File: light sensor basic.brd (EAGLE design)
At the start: 83.2 x 57.8 mm, 13 parts, among them J1 UJ2-MIBH-G-SMT-TR, U1 VCNT2020

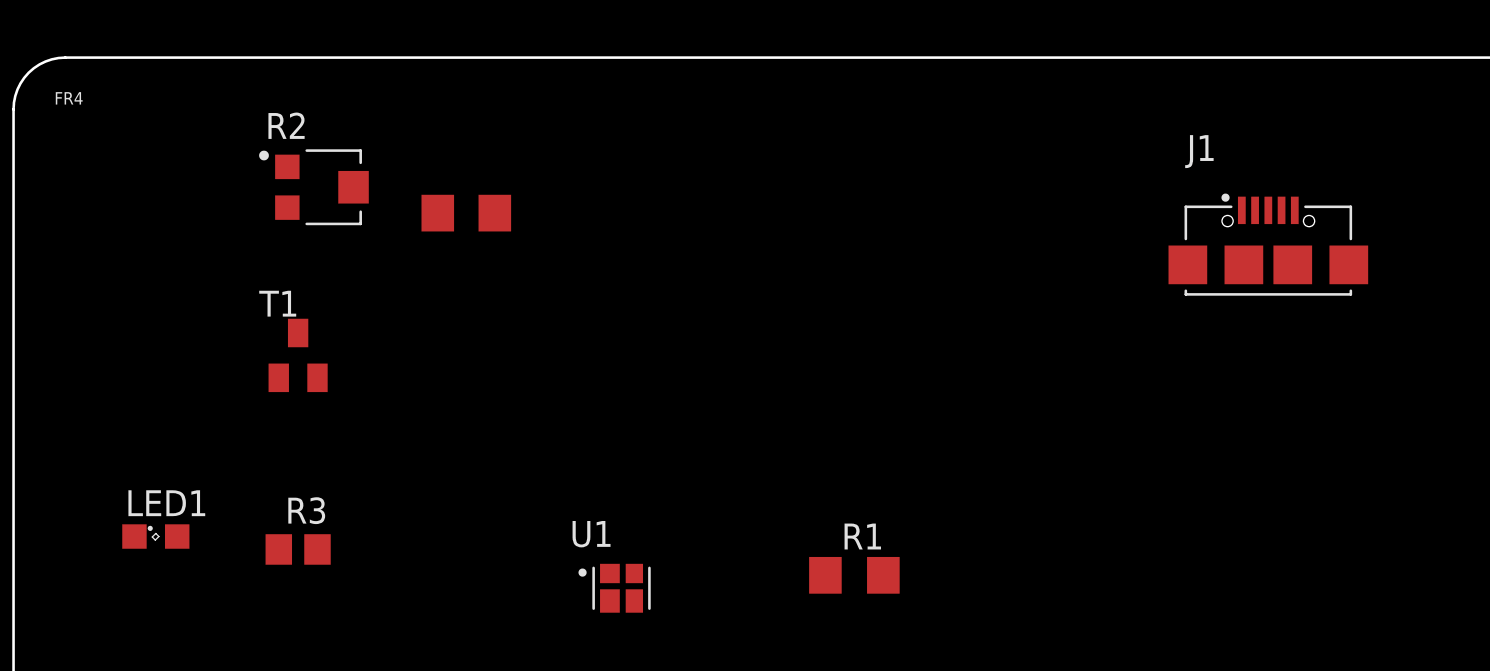
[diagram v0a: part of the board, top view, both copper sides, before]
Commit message: Update light sensor basic.brd
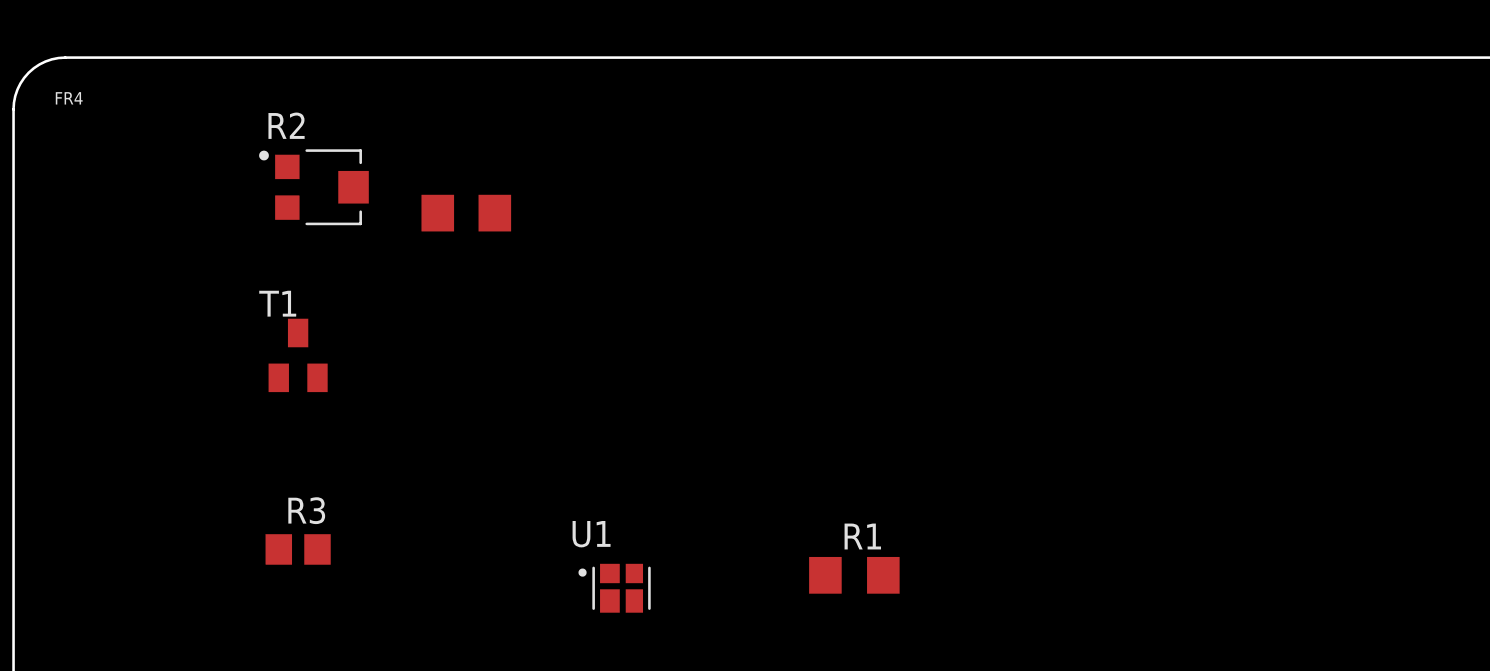
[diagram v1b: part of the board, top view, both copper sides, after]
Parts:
- removed J1: UJ2-MIBH-G-SMT-TR, UJ2-MIBH-G-SMT-TR:CUI_UJ2-MIBH-G-SMT-TR
- removed LED1: (no value), led:SML0805
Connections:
- net GND: no longer J1.5, J1.S1, J1.S2, J1.S3, J1.S4
- net N$4: no longer LED1.C
- net VCC: no longer J1.1
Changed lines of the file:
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@@
 <drawing>
 <settings>
-<setting alwaysvectorfont="no"/>
+<setting alwaysvectorfont="yes"/>
 <setting verticaltext="up"/>
 </settings>
@@
 <attribute name="VALUE" x="12.065" y="40.005" size="1.27" layer="27"/>
 </element>
-<element name="LED1" library="led" library_urn="urn:adsk.eagle:library:259" package="SML0805" package3d_urn="urn:adsk.eagle:package:15830/1" value="" x="6.985" y="34.29" smashed="yes">
-<attribute name="NAME" x="5.485" y="35.29" size="1.27" layer="25"/>
-<attribute name="POPULARITY" value="17" x="6.985" y="34.29" size="1.778" layer="27" display="off"/>
-<attribute name="VALUE" x="5.485" y="32.29" size="1.27" layer="27"/>
-</element>
 <element name="R3" library="rcl" library_urn="urn:adsk.eagle:library:334" package="R0805" package3d_urn="urn:adsk.eagle:package:23553/2" value="150" x="13.97" y="33.655" smashed="yes">
 <attribute name="NAME" x="13.335" y="34.925" size="1.27" layer="25"/>
@@
 <attribute name="SPICEPREFIX" value="R" x="13.97" y="33.655" size="1.778" layer="27" display="off"/>
 <attribute name="VALUE" x="13.335" y="31.115" size="1.27" layer="27"/>
-</element>
-<element name="J1" library="UJ2-MIBH-G-SMT-TR" package="CUI_UJ2-MIBH-G-SMT-TR" value="UJ2-MIBH-G-SMT-TR" x="61.595" y="47.625" smashed="yes">
-<attribute name="MANUFACTURER" value="CUI" x="61.595" y="47.625" size="1.778" layer="27" display="off"/>
-<attribute name="MAXIMUM_PACKAGE_HEIGHT" value="2.95 mm" x="61.595" y="47.625" size="1.778" layer="27" display="off"/>
-<attribute name="NAME" x="57.595" y="52.725" size="1.27" layer="25"/>
-<attribute name="PARTREV" value="1.0" x="61.595" y="47.625" size="1.778" layer="27" display="off"/>
-<attribute name="STANDARD" value="Manufacturer Recommendations" x="61.595" y="47.625" size="1.778" layer="27" display="off"/>
-<attribute name="VALUE" x="57.595" y="51.325" size="1.27" layer="27"/>
 </element>
 <element name="TP3" library="rcl" library_urn="urn:adsk.eagle:library:334" package="R1206" package3d_urn="urn:adsk.eagle:package:23540/2" value="" x="14.605" y="17.145" smashed="yes">
@@
 <contactref element="U1" pad="2"/>
 <contactref element="R3" pad="1"/>
-<contactref element="J1" pad="1"/>
 <contactref element="TP3" pad="1"/>
 <contactref element="TP3" pad="2"/>
 <wire x1="29.275" y1="31.125" x2="42.697" y2="32.385" width="0" layer="19" extent="1-1"/>
-<wire x1="60.295" y1="50.3" x2="29.275" y2="31.125" width="0" layer="19" extent="1-1"/>
-<wire x1="13.02" y1="33.655" x2="60.295" y2="50.3" width="0" layer="19" extent="1-1"/>
-<wire x1="16.027" y1="17.145" x2="60.295" y2="50.3" width="0" layer="19" extent="1-1"/>
-<wire x1="13.183" y1="17.145" x2="16.027" y2="17.145" width="0" layer="19" extent="1-1"/>
+<wire x1="13.02" y1="33.655" x2="29.275" y2="31.125" width="0" layer="19" extent="1-1"/>
+<wire x1="13.183" y1="17.145" x2="13.02" y2="33.655" width="0" layer="19" extent="1-1"/>
+<wire x1="16.027" y1="17.145" x2="13.183" y2="17.145" width="0" layer="19" extent="1-1"/>
 <wire x1="23.625" y1="50.165" x2="13.02" y2="33.655" width="0" layer="19" extent="1-1"/>
 </signal>
@@
 <contactref element="R2" pad="3"/>
 <contactref element="T1" pad="E"/>
-<contactref element="J1" pad="5"/>
-<contactref element="J1" pad="S3"/>
-<contactref element="J1" pad="S4"/>
-<contactref element="J1" pad="S1"/>
-<contactref element="J1" pad="S2"/>
 <contactref element="TP4" pad="1"/>
 <contactref element="TP4" pad="2"/>
-<wire x1="16.027" y1="12.7" x2="13.183" y2="12.7" width="0" layer="19" extent="1-1"/>
-<wire x1="57.645" y1="47.625" x2="13.183" y2="12.7" width="0" layer="19" extent="1-1"/>
-<wire x1="60.395" y1="47.625" x2="57.645" y2="47.625" width="0" layer="19" extent="1-1"/>
-<wire x1="62.795" y1="47.625" x2="60.395" y2="47.625" width="0" layer="19" extent="1-1"/>
-<wire x1="62.895" y1="50.3" x2="62.795" y2="47.625" width="0" layer="19" extent="1-1"/>
-<wire x1="65.545" y1="47.625" x2="62.795" y2="47.625" width="0" layer="19" extent="1-1"/>
-<wire x1="13.02" y1="42.08" x2="62.895" y2="50.3" width="0" layer="19" extent="1-1"/>
-<wire x1="13.44" y1="50.435" x2="13.02" y2="42.08" width="0" layer="19" extent="1-1"/>
-<wire x1="20.825" y1="50.165" x2="13.44" y2="50.435" width="0" layer="19" extent="1-1"/>
-<wire x1="30.475" y1="31.125" x2="20.825" y2="50.165" width="0" layer="19" extent="1-1"/>
+<wire x1="13.44" y1="50.435" x2="20.825" y2="50.165" width="0" layer="19" extent="1-1"/>
+<wire x1="13.02" y1="42.08" x2="13.44" y2="50.435" width="0" layer="19" extent="1-1"/>
+<wire x1="30.475" y1="31.125" x2="13.02" y2="42.08" width="0" layer="19" extent="1-1"/>
+<wire x1="16.027" y1="12.7" x2="30.475" y2="31.125" width="0" layer="19" extent="1-1"/>
+<wire x1="13.183" y1="12.7" x2="16.027" y2="12.7" width="0" layer="19" extent="1-1"/>
 </signal>
 <signal name="N$2">
@@
 <signal name="N$4">
 <contactref element="T1" pad="C"/>
-<contactref element="LED1" pad="C"/>
-<wire x1="13.97" y1="44.28" x2="5.935" y2="34.29" width="0" layer="19" extent="1-1"/>
 </signal>
 </signals>
